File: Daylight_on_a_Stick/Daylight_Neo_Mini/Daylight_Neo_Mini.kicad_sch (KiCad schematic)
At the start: 20 parts

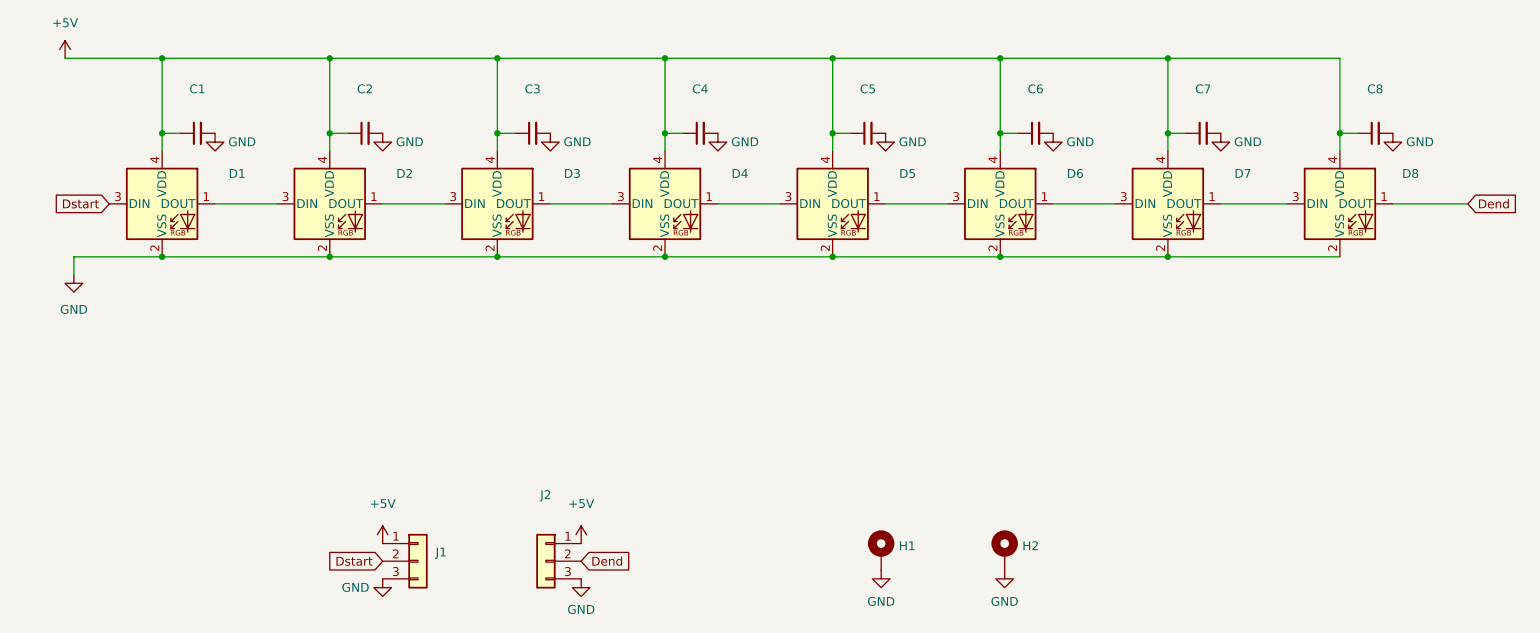
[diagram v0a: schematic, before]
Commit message: Fixed some Layout LED footprint issues
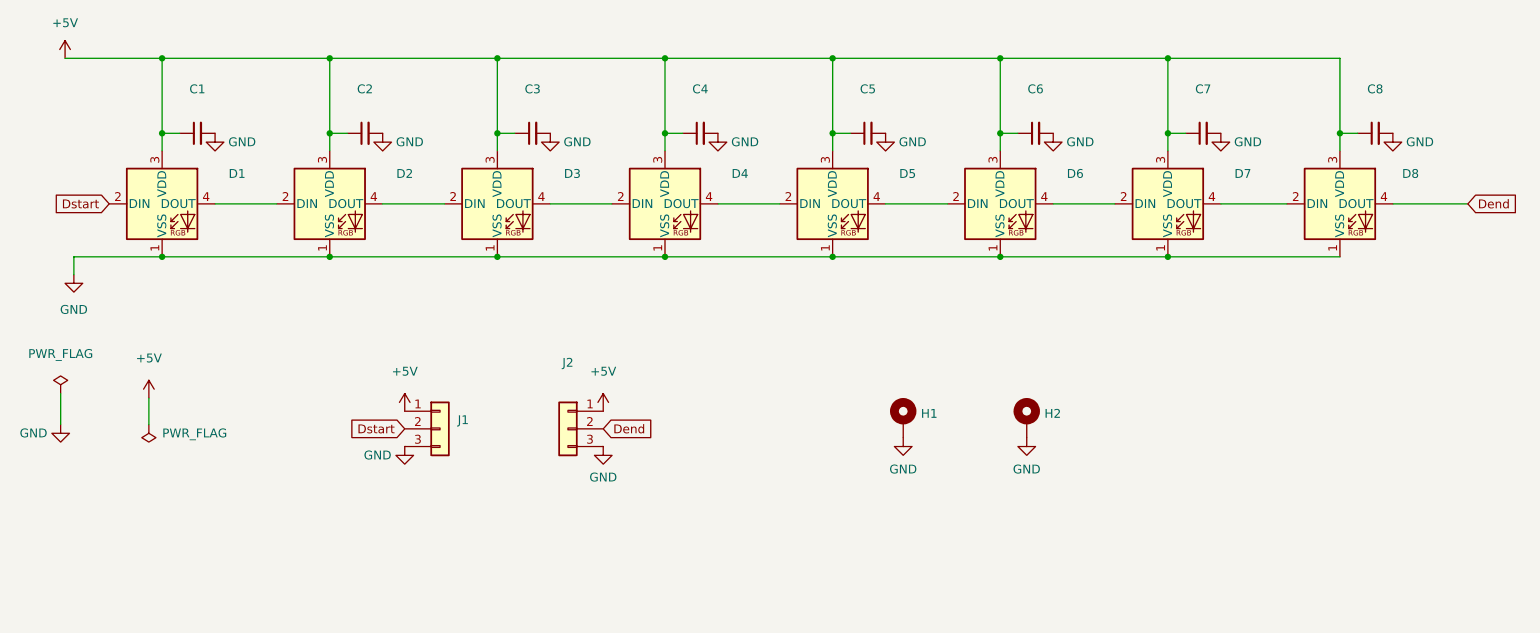
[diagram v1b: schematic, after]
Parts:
- C1, C2, C3, C4, C5, C6, C7, C8: LCSC C24497 -> C28233
- D1, D2, D3, D4, D5, D6, D7, D8: symbol LED:SK6812MINI -> LED:SK6812
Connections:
- net +5V: now also D1.3 (VDD), D2.3 (VDD), D3.3 (VDD), D4.3 (VDD), D5.3 (VDD), D6.3 (VDD), D7.3 (VDD), D8.3 (VDD); no longer D1.4 (VDD), D2.4 (VDD), D3.4 (VDD), D4.4 (VDD), D5.4 (VDD), D6.4 (VDD), D7.4 (VDD), D8.4 (VDD)
- net Dend: now also D8.4 (DOUT); no longer D8.1 (DOUT)
- net Dstart: now also D1.2 (DIN); no longer D1.3 (DIN)
- net GND: now also D1.1 (VSS), D2.1 (VSS), D3.1 (VSS), D4.1 (VSS), D5.1 (VSS), D6.1 (VSS), D7.1 (VSS), D8.1 (VSS); no longer D1.2 (VSS), D2.2 (VSS), D3.2 (VSS), D4.2 (VSS), D5.2 (VSS), D6.2 (VSS), D7.2 (VSS), D8.2 (VSS)
- new net: D2.4 (DOUT), D3.2 (DIN)
- new net: D3.4 (DOUT), D4.2 (DIN)
- new net: D1.4 (DOUT), D2.2 (DIN)
- new net: D4.4 (DOUT), D5.2 (DIN)
- new net: D5.4 (DOUT), D6.2 (DIN)
- new net: D6.4 (DOUT), D7.2 (DIN)
- new net: D7.4 (DOUT), D8.2 (DIN)
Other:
- moved on the sheet: H1, H2, J1, J2

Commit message: Minor LED Updates
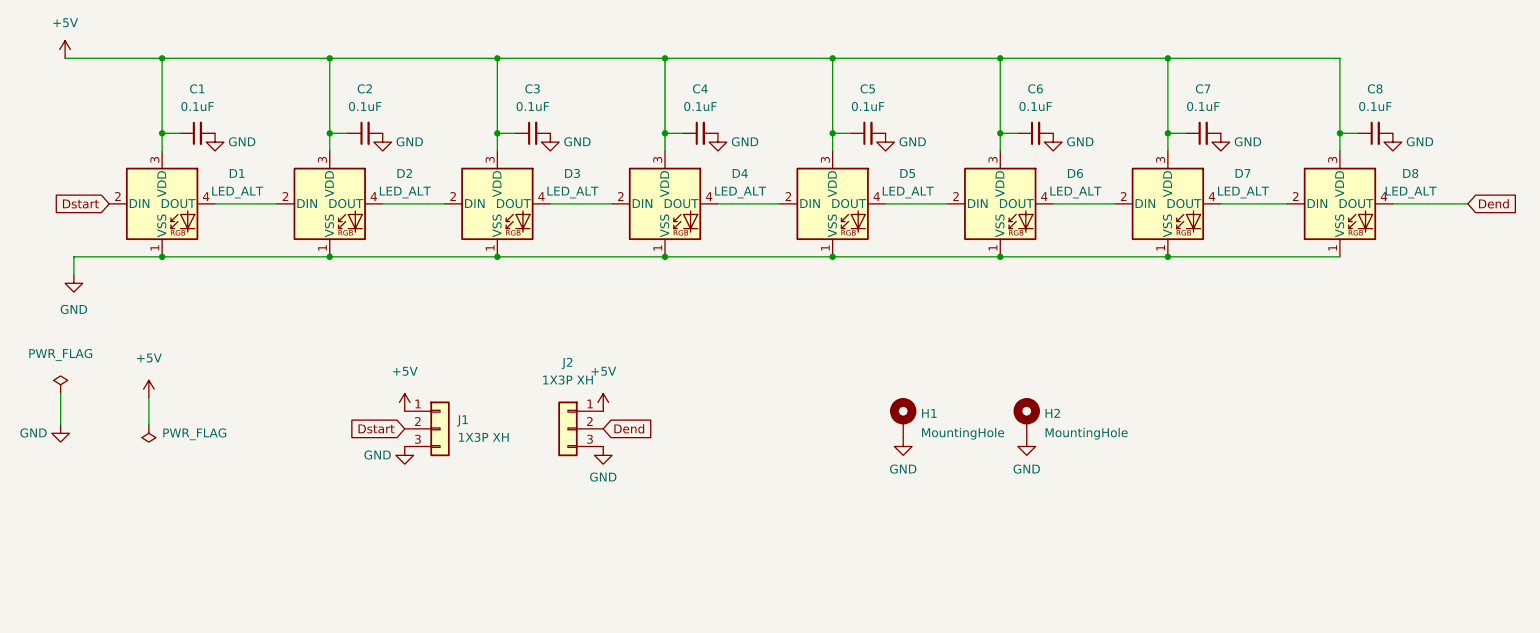
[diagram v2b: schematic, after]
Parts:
- C1, C2, C3, C4, C5, C6, C7, C8: value (none) -> 0.1uF; footprint (none) -> Daylight:C_0805_2012Metric_Pad1.18x1.45mm_HandSolder_V3Dspec
- D1, D2, D3, D4, D5, D6, D7, D8: value (none) -> LED_ALT; footprint (none) -> Daylight:XL-3528RGBW-WS2812B
- H1, H2: value (none) -> MountingHole; footprint (none) -> MountingHole:MountingHole_3.2mm_M3_Pad_Via
- J1, J2: value (none) -> 1X3P XH; footprint (none) -> Connector_JST:JST_XH_S3B-XH-A_1x03_P2.50mm_Horizontal; LCSC (none) -> C2908612
